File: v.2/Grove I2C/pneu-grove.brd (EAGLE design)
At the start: 30.5 x 50.8 mm, 13 parts, among them J1 TWIG-2.0-DIP, J12 A3, J4 TWIG-2.0-DIP, J5 TWIG-2.0-DIP, U2 NCP1117-5

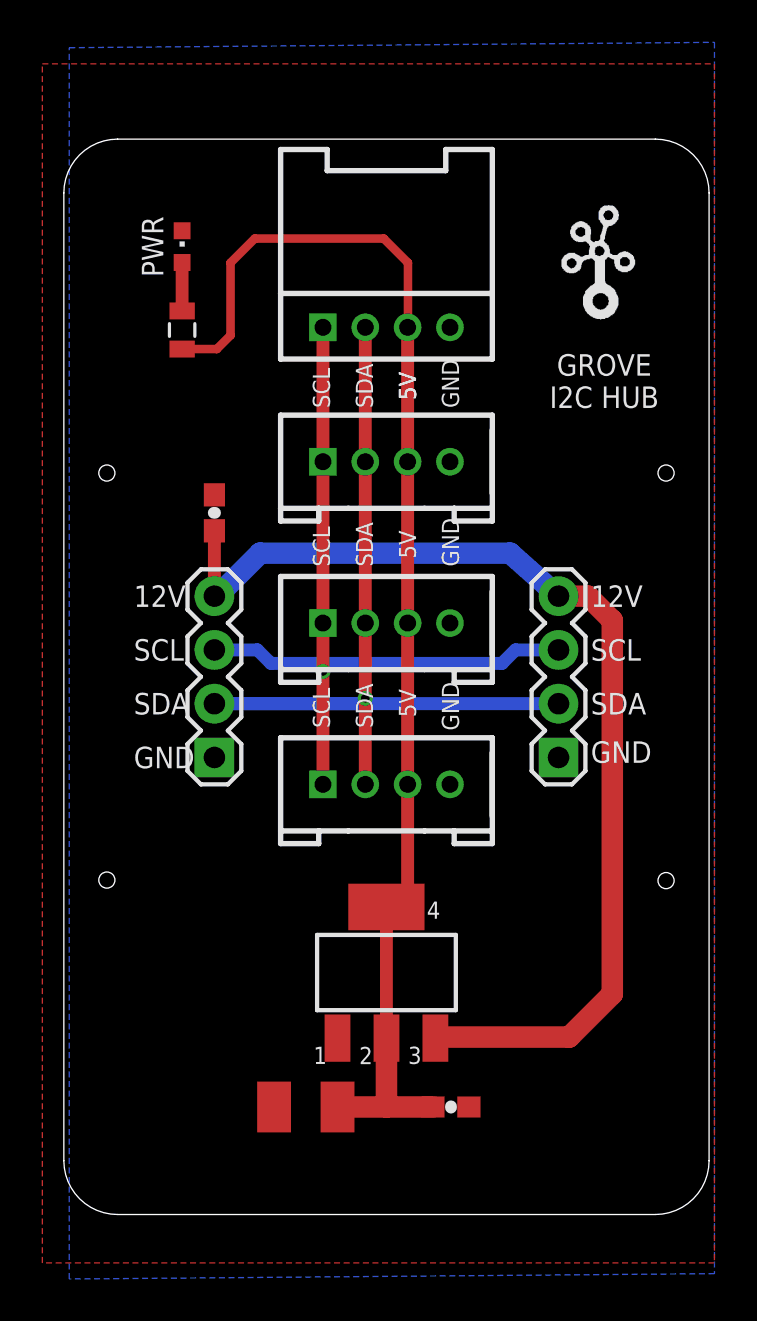
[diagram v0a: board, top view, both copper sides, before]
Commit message: minor changes
getting ready for production:

correct indicator led position on master board
add corner drills to slave boards
generate silk screens
adjust edge connector distance for better fit
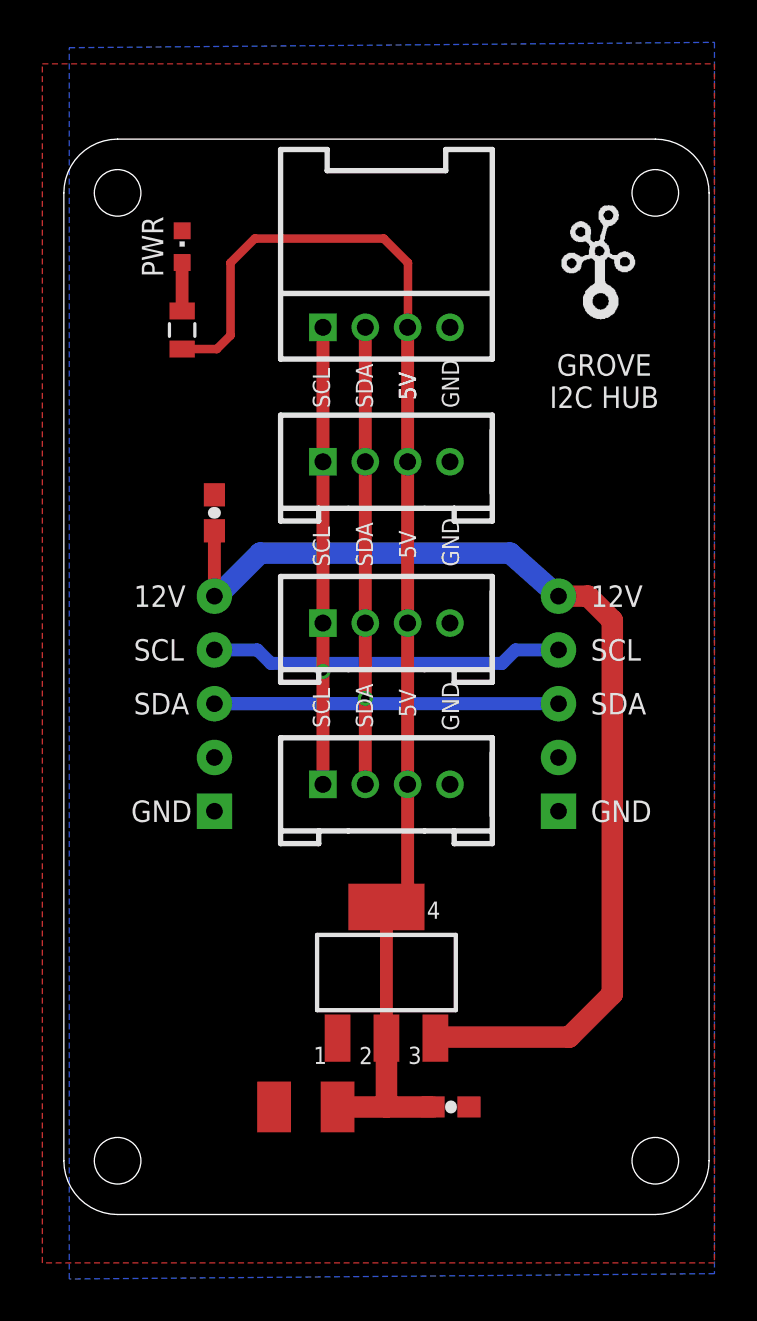
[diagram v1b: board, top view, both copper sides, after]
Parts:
- removed JP2, JP3: (no value), SparkFun-Connectors:1X04
- added U$23, U$24: 1X05, digikey:1X05_TIGHT
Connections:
- net GND: now also U$23.P$5, U$24.P$5; no longer JP2.1, JP3.1
- net SCL: now also U$23.P$3, U$24.P$3; no longer JP2.3, JP3.3
- net SDA: now also U$23.P$2, U$24.P$2; no longer JP2.2, JP3.2
- net VIN: now also U$23.P$1, U$24.P$1; no longer JP2.4, JP3.4
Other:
- board text added: "07/19/2016"
- board text removed: "10/27/2015"
